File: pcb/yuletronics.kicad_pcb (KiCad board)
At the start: 2 copper layers, 45 x 50 mm, 35 parts, among them IC1 STM32F042F6P6, IC2 MCP1700, IC3 TLV61225, J1 BATT, J2 MICROUSB, P1 SWD_TC, SW1 BOOTLOAD, SW2 PWR_SWITCH

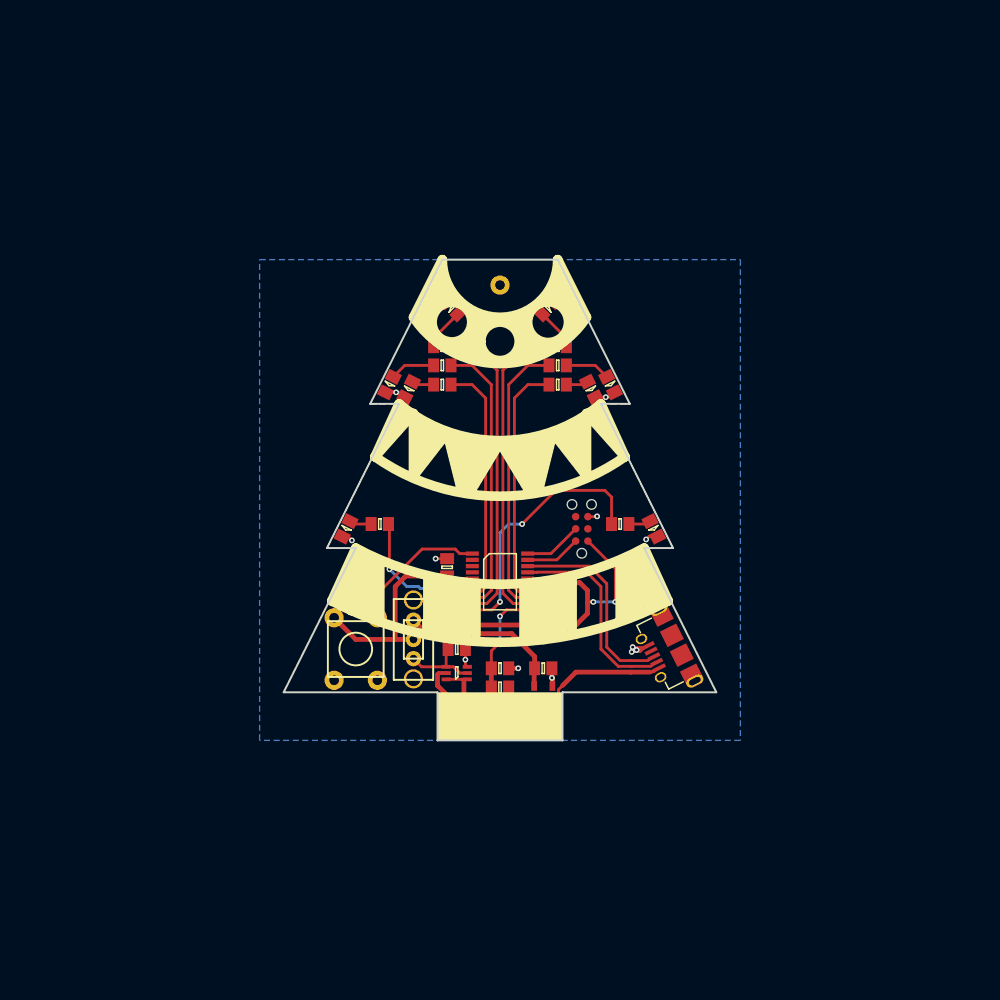
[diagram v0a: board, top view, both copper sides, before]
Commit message: More LEDs, MOSFETs, board outline
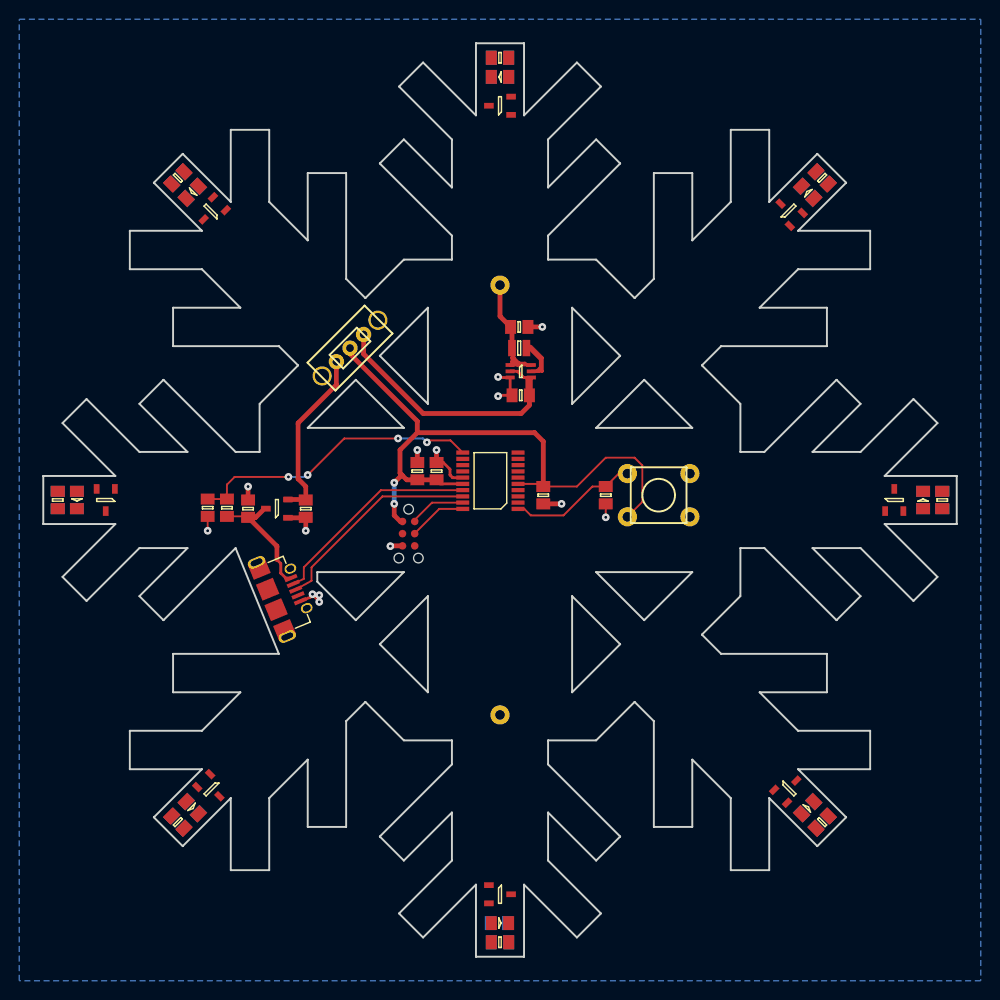
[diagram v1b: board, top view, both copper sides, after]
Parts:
- added D10: LED, agg:0805-LED, F.Cu at (162.0, 78.0)
- added D11: LED, agg:0805-LED, F.Cu at (86.0, 110.0)
- added D12: LED, agg:0805-LED, F.Cu at (130.0, 66.0)
- added D13: LED, agg:0805-LED, B.Cu at (98.0, 142.0)
- added D14: LED, agg:0805-LED, B.Cu at (162.0, 78.0)
- added D15: LED, agg:0805-LED, B.Cu at (86.0, 110.0)
- added D16: LED, agg:0805-LED, B.Cu at (130.0, 66.0)
- added D9: LED, agg:0805-LED, F.Cu at (98.0, 142.0)
- added Q1: BSS138P, agg:SOT-23, F.Cu at (100.0, 80.0)
- added Q2: BSS138P, agg:SOT-23, F.Cu at (160.0, 140.0)
- added Q3: BSS138P, agg:SOT-23, F.Cu at (130.0, 151.0)
- added Q4: BSS138P, agg:SOT-23, F.Cu at (171.0, 110.0)
- added Q5: BSS138P, agg:SOT-23, F.Cu at (100.0, 140.0)
- added Q6: BSS138P, agg:SOT-23, F.Cu at (160.0, 80.0)
- added Q7: BSS138P, agg:SOT-23, F.Cu at (89.0, 110.0)
- added Q8: BSS138P, agg:SOT-23, F.Cu at (130.0, 69.0)
- added R12: 10, agg:0805, F.Cu at (96.5, 143.5)
- added R13: 10, agg:0805, F.Cu at (163.5, 76.5)
- added R14: 10, agg:0805, F.Cu at (84.0, 110.0)
- added R15: 10, agg:0805, F.Cu at (130.0, 64.0)
- added R16: 10, agg:0805, B.Cu at (96.5, 143.5)
- added R17: 10, agg:0805, B.Cu at (163.5, 76.5)
- added R18: 10, agg:0805, B.Cu at (84.0, 110.0)
- added R19: 10, agg:0805, B.Cu at (130.0, 64.0)
- D5, D6, D7, D8: moved to B.Cu
- R10, R11, R8, R9: value R -> 10; moved to B.Cu
- R4, R5, R6, R7: value R -> 10
- moved R10 60.3 mm to (130.0, 156.0), turned to 180 degrees
- moved R6 60.3 mm to (130.0, 156.0)
- moved R5 60.3 mm to (163.5, 143.5), turned to 225 degrees
- moved D2 60.1 mm to (162.0, 142.0), turned to 225 degrees
- moved D5 59.4 mm to (98.0, 78.0), turned to 45 degrees
- moved D6 58.6 mm to (162.0, 142.0)
- moved R8 58.4 mm to (96.5, 76.5), turned to 45 degrees
- moved D7 57.2 mm to (129.9, 154.0), turned to 180 degrees
- moved D3 57.2 mm to (130.0, 154.0), turned to 180 degrees
- moved R9 56.6 mm to (163.5, 143.5), turned to 225 degrees
- moved R7 54.4 mm to (176.0, 110.0), turned to 270 degrees
- moved D4 52.9 mm to (174.0, 110.0), turned to 270 degrees
- moved J2 42.4 mm to (106.3, 120.3), turned to 292.5 degrees
- moved C4 42.0 mm to (132.0, 92.0), turned to 0 degrees
- moved R11 41.8 mm to (176.0, 110.0), turned to 270 degrees
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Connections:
- D1 pad 1: GND -> Net-(D1-Pad1)
- D2 pad 1: GND -> Net-(D2-Pad1)
- D3 pad 1: GND -> Net-(D3-Pad1)
- D4 pad 1: GND -> Net-(D4-Pad1)
- D5 pad 1: GND -> Net-(D1-Pad1)
- D6 pad 1: GND -> Net-(D2-Pad1)
- D7 pad 1: GND -> Net-(D3-Pad1)
- D8 pad 1: GND -> Net-(D4-Pad1)
- IC1 pad 2: Net-(IC1-Pad2) -> (no net)
- IC1 pad 3: Net-(IC1-Pad3) -> (no net)
- IC1 pad 4: Net-(IC1-Pad4) -> (no net)
- J2 pad 4: Net-(J2-Pad4) -> (no net)
- J2 pad S: Net-(J2-PadS) -> (no net)
- P1 pad 3: Net-(P1-Pad3) -> (no net)
- P1 pad 6: Net-(P1-Pad6) -> (no net)
- R10 pad 1: /LED7 -> 3v3
- R11 pad 1: /LED8 -> 3v3
- R4 pad 1: /LED1 -> 3v3
- R5 pad 1: /LED2 -> 3v3
- R6 pad 1: /LED3 -> 3v3
- R7 pad 1: /LED4 -> 3v3
- R8 pad 1: /LED5 -> 3v3
- R9 pad 1: /LED6 -> 3v3
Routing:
- net /LED6: track 32.1 -> 0.00 mm
- net /LED4: track 32.1 -> 0.00 mm
- net /LED7: track 28.7 -> 0.00 mm
- net /LED3: track 28.7 -> 0.00 mm
- net /LED5: track 26.9 -> 0.00 mm, vias 2 -> 0
- net /LED8: track 25.4 -> 0.00 mm
- net /LED2: track 25.4 -> 0.00 mm
- net /BATT_3V3: track 8.15 -> 30.8 mm
- net /USB_DETECT: track 10.9 -> 30.8 mm, vias 2 -> 4
- net /LED1: track 14.4 -> 0.00 mm, vias 2 -> 0
- net 5v: track 23.0 -> 13.3 mm
- net Net-(IC3-Pad5): track 4.34 -> 9.34 mm
- net /VBATT: track 11.3 -> 16.3 mm
- net GND: track 31.6 -> 26.8 mm, vias 18 -> 14
- net Net-(D7-Pad2): track 4.69 -> 0.00 mm
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- removed copper zone on F.Cu, net (none)
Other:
- board size 45 x 50 mm -> 95 x 95 mm
- net class Default: clearance 0.15 -> 0.2; trace_width 0.15 -> 0.2; via_dia 0.6 -> 0.8
- rule trace_clearance: 0.15 -> 0.2

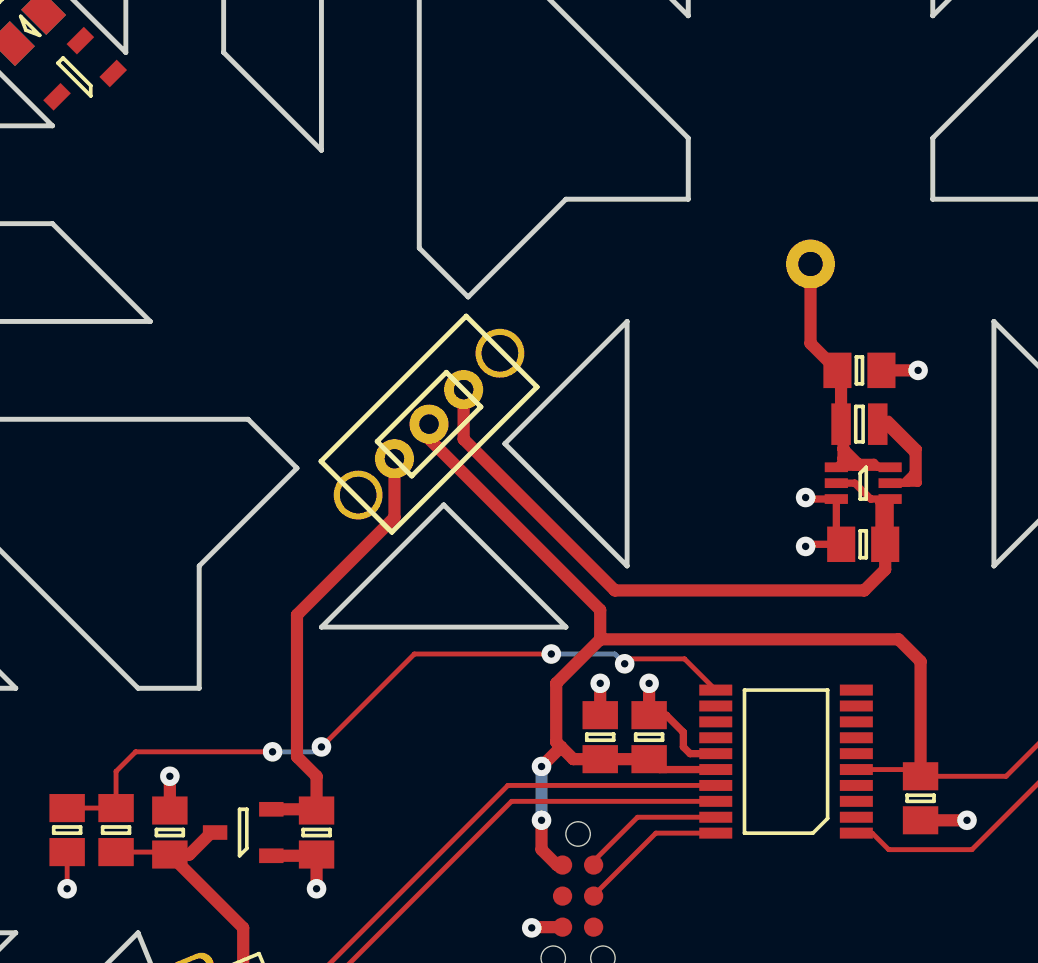
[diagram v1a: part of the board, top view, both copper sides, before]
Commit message: Partially did new 5V bus
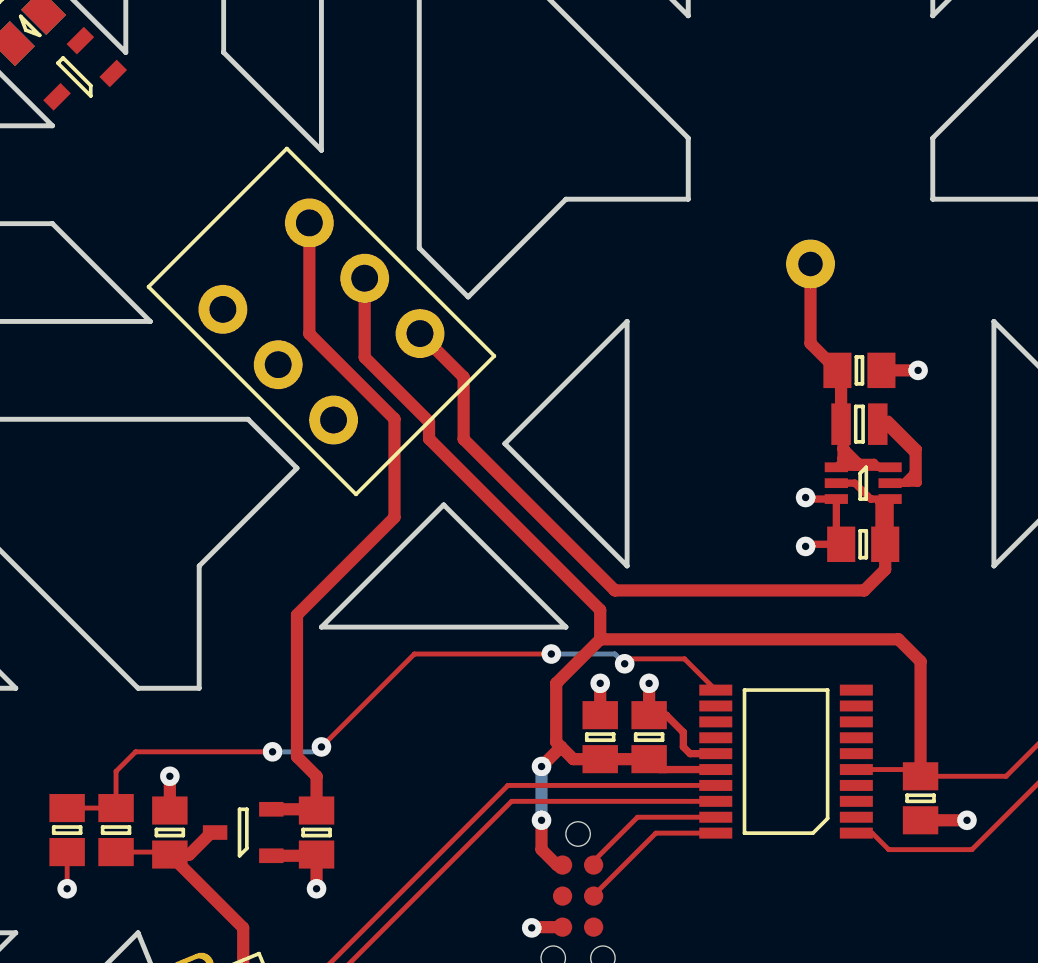
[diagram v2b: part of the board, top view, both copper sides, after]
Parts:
- removed SW2: PWR_SWITCH, agg:SPDT_SWITCH
- added U1: dpdt, agg:dpdt, F.Cu at (110.0, 90.0)
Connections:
- J1 pad 2: /VBATT -> Net-(J1-Pad2)
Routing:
- net /USB_3V3: track 18.2 -> 29.3 mm
- net 3v3: track 68.2 -> 75.2 mm
- net /VBATT: track 16.3 -> 13.0 mm
- net Net-(J1-Pad2): track 0.00 -> 3.25 mm
- net /BATT_3V3: track 30.8 -> 33.8 mm

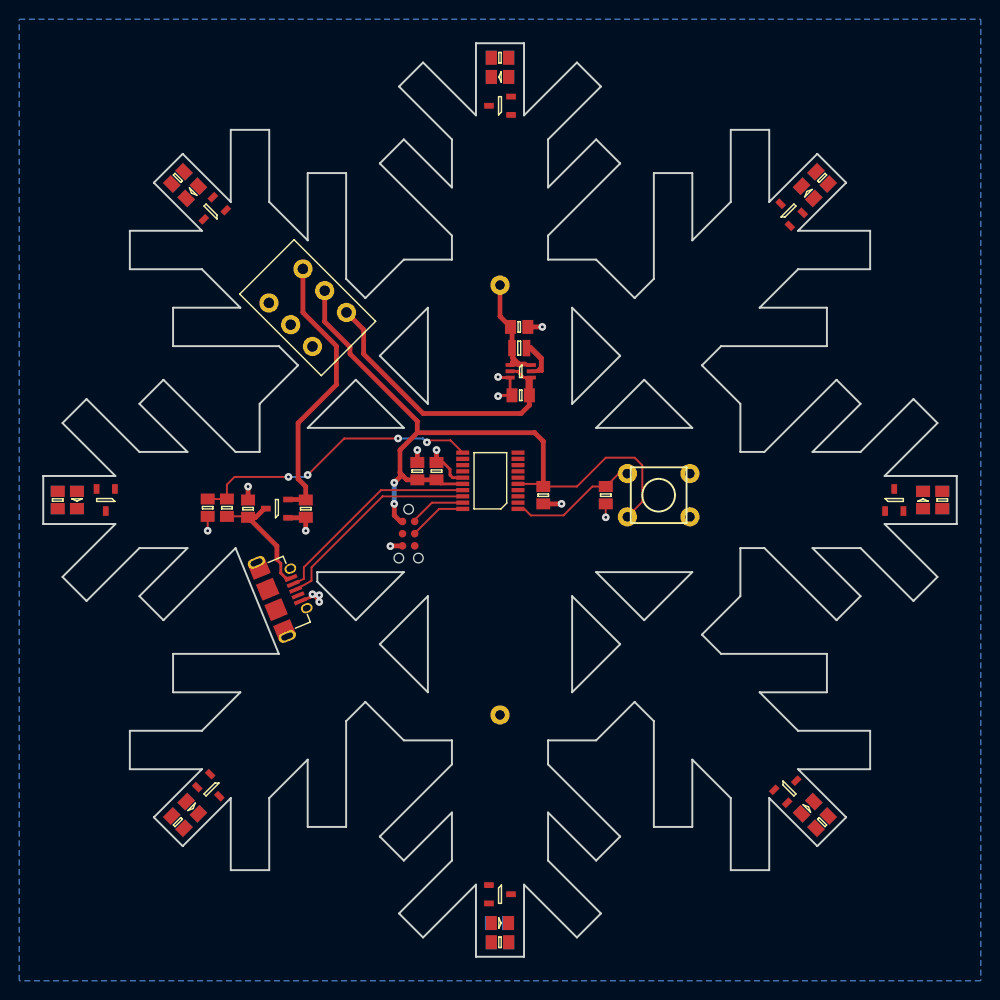
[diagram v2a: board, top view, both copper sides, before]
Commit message: Added FET pulldowns, placed and routed
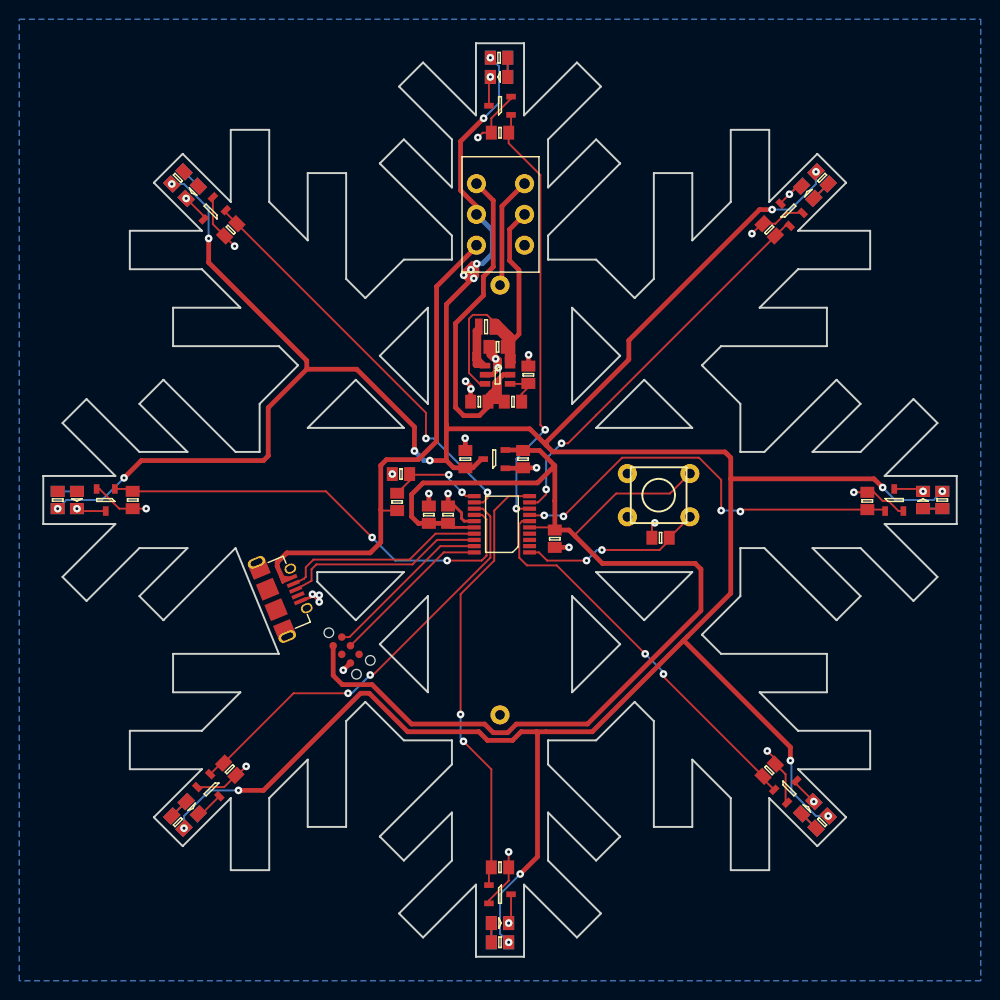
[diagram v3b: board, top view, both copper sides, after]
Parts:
- added R20: 100, agg:0805, F.Cu at (129.9, 64.0)
- added R21: 100, agg:0805, B.Cu at (129.9, 64.0)
- added R22: 10k, agg:0805, F.Cu at (102.0, 81.9)
- added R23: 10k, agg:0805, F.Cu at (101.9, 138.0)
- added R24: 10k, agg:0805, F.Cu at (158.0, 138.1)
- added R25: 10k, agg:0805, F.Cu at (158.0, 81.9)
- added R26: 10k, agg:0805, F.Cu at (130.0, 148.2)
- added R27: 10k, agg:0805, F.Cu at (91.8, 110.0)
- added R28: 10k, agg:0805, F.Cu at (168.2, 110.1)
- added R29: 10k, agg:0805, F.Cu at (130.0, 71.8)
- IC3: value TLV61225 -> TLV61220; footprint agg:SC-70-6 -> agg:SOT-23-6
- R10, R16, R18, R8: value 10 -> 100; moved to F.Cu
- R11, R14, R17, R19, R4, R6, R9: value 10 -> 100
- R12, R13: value 10 -> R
- R15, R5, R7: value 10 -> 100; moved to B.Cu
- moved R5 94.8 mm to (96.5, 76.5), turned to 45 degrees
- moved R8 94.8 mm to (163.5, 143.5), turned to 225 degrees
- moved R15 92.0 mm to (130.0, 156.0), turned to 180 degrees
- moved R18 92.0 mm to (176.0, 110.0), turned to 270 degrees
- moved R10 86.3 mm to (163.5, 76.5), turned to 315 degrees
- moved R17 86.3 mm to (84.0, 110.0), turned to 90 degrees
- moved R7 86.3 mm to (96.5, 143.5), turned to 135 degrees
- moved R14 65.1 mm to (130.0, 156.0), turned to 180 degrees
- moved R19 65.1 mm to (176.0, 110.0), turned to 270 degrees
- moved R12 55.9 mm to (131.3, 99.8), turned to 0 degrees
- moved R13 36.8 mm to (132.9, 97.0), turned to 90 degrees
- moved R11 35.8 mm to (163.5, 76.5), turned to 315 degrees
- moved R16 35.8 mm to (84.0, 110.0), turned to 90 degrees
- moved R6 35.8 mm to (96.5, 143.5), turned to 135 degrees
- moved C5 23.2 mm to (126.4, 105.8)
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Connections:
- C6 pad 1: /USB_3V3 -> 3v3
- C7 pad 1: /BATT_3V3 -> /BATT_5V
- IC1 pad 12: /LED6 -> /LED1
- IC1 pad 13: /LED7 -> /LED2
- IC1 pad 14: /LED8 -> /LED6
- IC1 pad 6: /LED1 -> /LED3
- IC1 pad 7: /LED2 -> /LED7
- IC1 pad 8: /LED3 -> /LED8
- IC2 pad 2: /USB_3V3 -> 3v3
- IC3 pad 1: /VBATT -> Net-(IC3-Pad1)
- IC3 pad 2: /BATT_3V3 -> GND
- IC3 pad 3: GND -> /VBATT
- IC3 pad 4: /BATT_3V3 -> Net-(IC3-Pad4)
- IC3 pad 5: Net-(IC3-Pad5) -> /BATT_5V
- J2 pad 1: 5v -> /USB_5V
- L1 pad 2: Net-(IC3-Pad5) -> Net-(IC3-Pad1)
- R10 pad 1: 3v3 -> 5v
- R10 pad 2: Net-(D7-Pad2) -> Net-(D10-Pad2)
- R11 pad 1: 3v3 -> 5v
- R11 pad 2: Net-(D8-Pad2) -> Net-(D14-Pad2)
- R12 pad 1: 3v3 -> /BATT_5V
- R12 pad 2: Net-(D9-Pad2) -> Net-(IC3-Pad4)
- R13 pad 1: 3v3 -> Net-(IC3-Pad4)
- R13 pad 2: Net-(D10-Pad2) -> GND
- R14 pad 1: 3v3 -> 5v
- R14 pad 2: Net-(D11-Pad2) -> Net-(D3-Pad2)
- R15 pad 1: 3v3 -> 5v
- R15 pad 2: Net-(D12-Pad2) -> Net-(D7-Pad2)
- R16 pad 1: 3v3 -> 5v
- R16 pad 2: Net-(D13-Pad2) -> Net-(D11-Pad2)
- R17 pad 1: 3v3 -> 5v
- R17 pad 2: Net-(D14-Pad2) -> Net-(D15-Pad2)
- R18 pad 1: 3v3 -> 5v
- R18 pad 2: Net-(D15-Pad2) -> Net-(D4-Pad2)
- R19 pad 1: 3v3 -> 5v
- R19 pad 2: Net-(D16-Pad2) -> Net-(D8-Pad2)
- R2 pad 1: 5v -> /USB_5V
- R4 pad 1: 3v3 -> 5v
- R5 pad 1: 3v3 -> 5v
- R5 pad 2: Net-(D2-Pad2) -> Net-(D5-Pad2)
- R6 pad 1: 3v3 -> 5v
- R6 pad 2: Net-(D3-Pad2) -> Net-(D9-Pad2)
- R7 pad 1: 3v3 -> 5v
- R7 pad 2: Net-(D4-Pad2) -> Net-(D13-Pad2)
- R8 pad 1: 3v3 -> 5v
- R8 pad 2: Net-(D5-Pad2) -> Net-(D2-Pad2)
- R9 pad 1: 3v3 -> 5v
- U1 pad 4: /BATT_3V3 -> /BATT_5V
- U1 pad 5: 3v3 -> 5v
- U1 pad 6: /USB_3V3 -> /USB_5V
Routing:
- net 5v: track 13.3 -> 382.3 mm, vias 0 -> 22
- net /USB_5V: track 0.00 -> 57.5 mm
- net GND: track 26.8 -> 83.9 mm, vias 14 -> 24
- net 3v3: track 75.2 -> 125.7 mm, vias 2 -> 0
- net /LED6: track 0.00 -> 47.2 mm, vias 0 -> 2
- net /LED5: track 0.00 -> 46.1 mm, vias 0 -> 2
- net /LED8: track 0.00 -> 45.2 mm, vias 0 -> 2
- net /LED2: track 0.00 -> 44.8 mm, vias 0 -> 2
- net /BATT_5V: track 0.00 -> 44.7 mm
- net /LED7: track 0.00 -> 43.9 mm, vias 0 -> 4
- net /LED1: track 0.00 -> 43.2 mm, vias 0 -> 2
- net /LED3: track 0.00 -> 41.6 mm, vias 0 -> 2
- net /LED4: track 0.00 -> 41.1 mm, vias 0 -> 2
- net /VBATT: track 13.0 -> 49.6 mm
- net /BATT_3V3: track 33.8 -> 0.00 mm
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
